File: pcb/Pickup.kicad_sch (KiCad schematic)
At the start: 41 parts, among them IC1 MAX9924UAUB+, K1 AQY212EHAX, Q7 MMBT2222A, T1 SM-LP-5001E

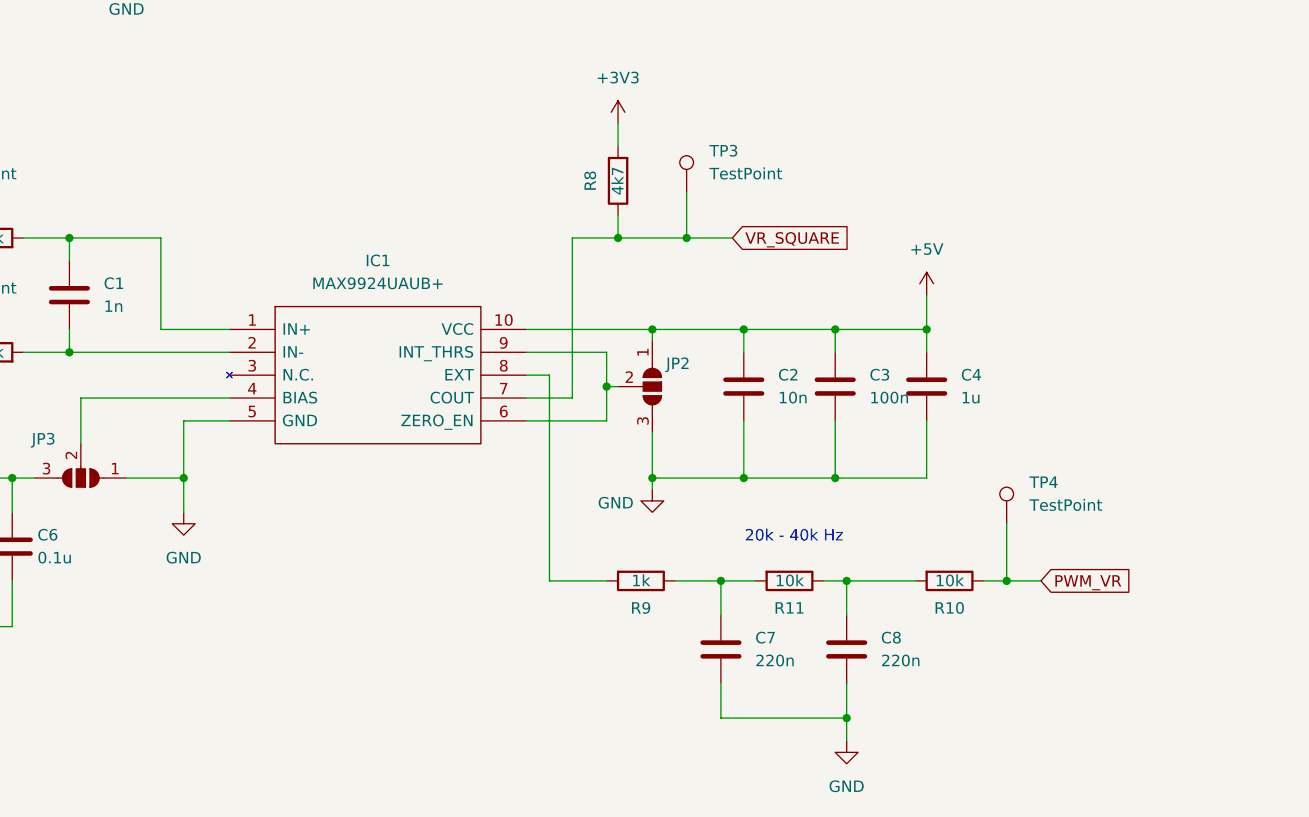
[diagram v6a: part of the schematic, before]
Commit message: External voltage reference of the MAX9924 is now a voltage divider and not the ESP32 PWM anymore
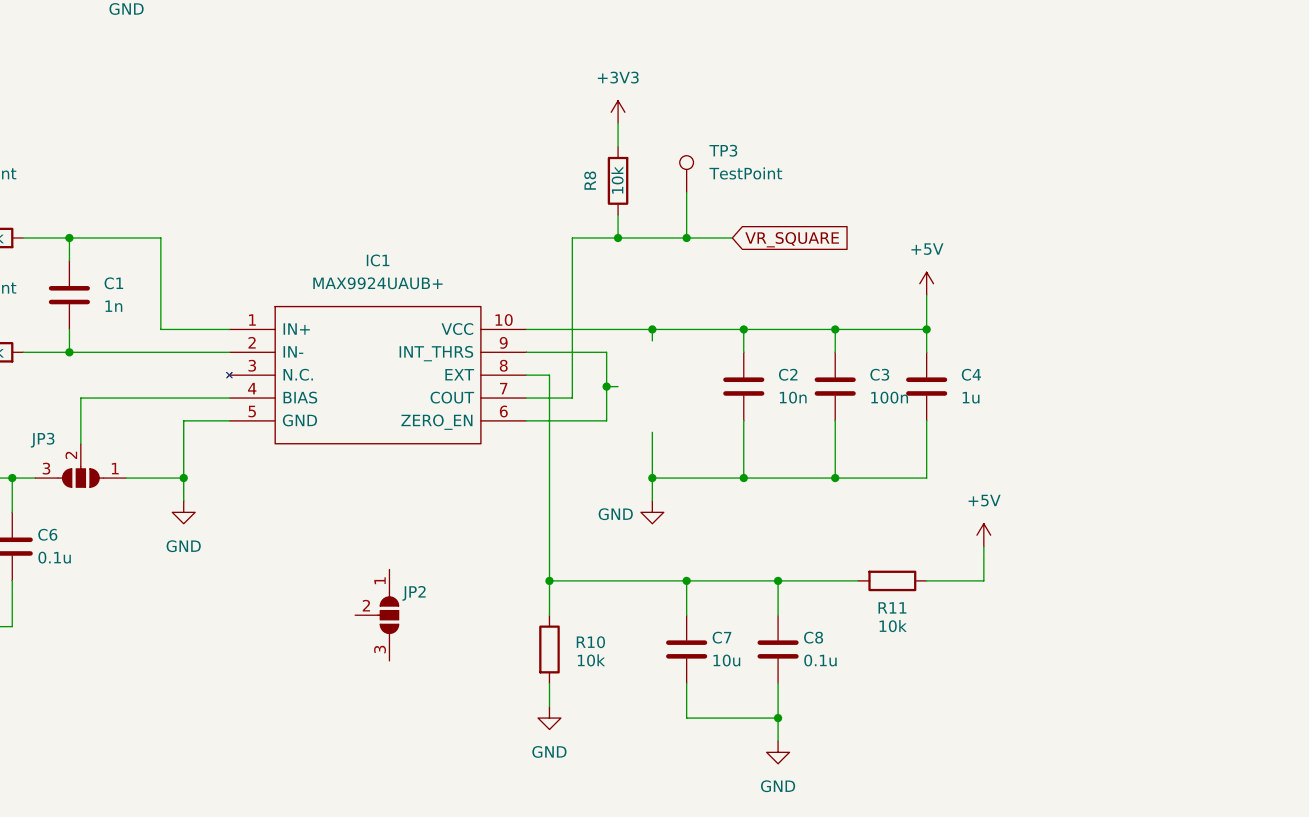
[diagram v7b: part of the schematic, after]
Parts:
- removed R9: 1k, Resistor_SMD:R_0603_1608Metric, symbol Device:R
- removed TP4: TestPoint, Connector_PinHeader_1.00mm:PinHeader_1x01_P1.00mm_Vertical, symbol Connector:TestPoint
- C7: value 220n -> 10u
- C8: value 220n -> 0.1u
- R8: value 4k7 -> 10k
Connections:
- net PWM_VR is gone; now on an unnamed net: R10.1
- net +5V: now also R11.1; no longer JP2.1 (A)
- net GND: now also R10.2; no longer JP2.3 (B)
- net at C7.1, R11.2: now also C8.1, IC1.8 (EXT)
- net at IC1.6 (ZERO_EN), IC1.9 (INT_THRS): no longer JP2.2 (C)
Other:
- note removed: "20k - 40k Hz"
- moved on the sheet: JP2, R10, R11

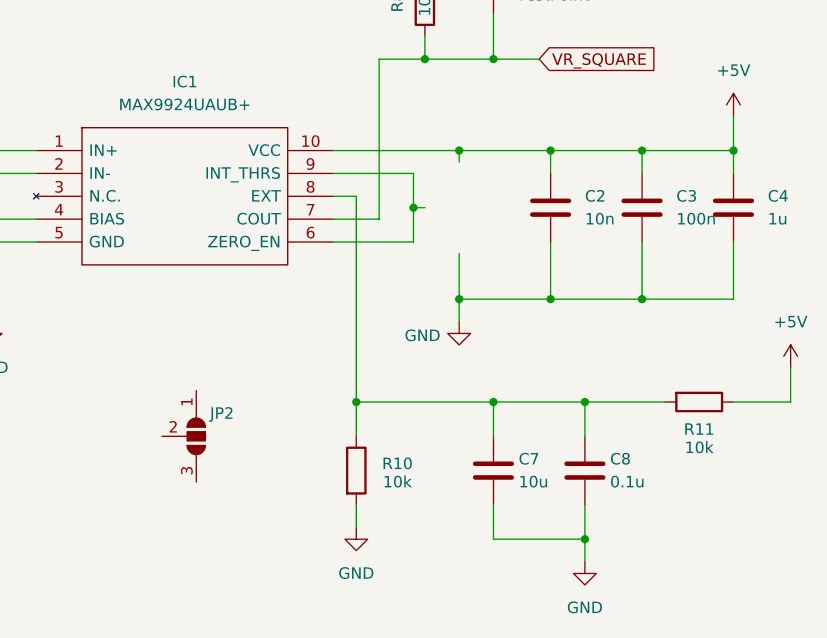
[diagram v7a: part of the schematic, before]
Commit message: removed mode A1 from MAX9924 configuration
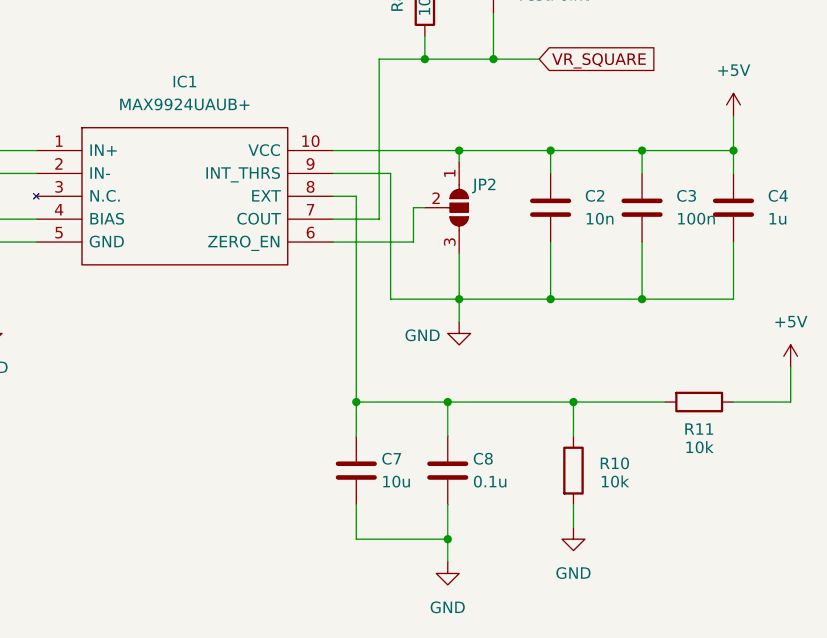
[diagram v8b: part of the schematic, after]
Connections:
- net +5V: now also JP2.1 (A)
- net GND: now also IC1.9 (INT_THRS), JP2.3 (B)
- net at IC1.6 (ZERO_EN): now also JP2.2 (C); no longer IC1.9 (INT_THRS)
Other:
- moved on the sheet: C7, C8, JP2, R10
